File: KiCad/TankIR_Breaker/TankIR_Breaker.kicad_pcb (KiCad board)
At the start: 2 copper layers, 44.6 x 18.2 mm, 16 parts, among them J1 VBATT, J2 TRIGGER, J3 SERVO, J4 RC, J5 APPLE, J6 SOUND, J7 IR_OUT, J8 MUZZLE, Q1 BC337, Q2 BC337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

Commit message: upd
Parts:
- moved R3 0.20 mm to (116.1, 70.7)
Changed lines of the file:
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@@
 	(footprint "Resistor_THT:R_Axial_DIN0204_L3.6mm_D1.6mm_P2.54mm_Vertical"
 		(layer "F.Cu")
-		(at 116.12 70.5 180)
+		(at 116.12 70.7 180)
 		(descr "Resistor, Axial_DIN0204 series, Axial, Vertical, pin pitch=2.54mm, 0.167W, length*diameter=3.6*1.6mm^2, http://cdn-reichelt.de/documents/datenblatt/B400/1_4W%23YAG.pdf")
 		(tags "Resistor Axial_DIN0204 series Axial Vertical pin pitch 2.54mm 0.167W length 3.6mm diameter 1.6mm")
 		(property "Reference" "R3"
-			(at 3.22 2 270)
+			(at 3.42 1.3 180)
 			(layer "F.SilkS")
 			(effects
@@
 		)
 	)
+	(gr_text "+"
+		(at 113.1 69 0)
+		(layer "F.SilkS")
+		(effects
+			(font
+				(size 1 1)
+				(thickness 0.2)
+				(bold yes)
+			)
+			(justify left bottom)
+		)
+	)
 	(gr_text "TRIG"
 		(at 92.1 63.1 90)
@@
 	)
 	(gr_text "+"
-		(at 96.4 63.9 0)
+		(at 90.7 64 0)
 		(layer "F.SilkS")
 		(effects

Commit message: fix
Fixed missing 5V connection
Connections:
- A1 pad 27: unconnected-(A1-+5V-Pad27) -> 5V

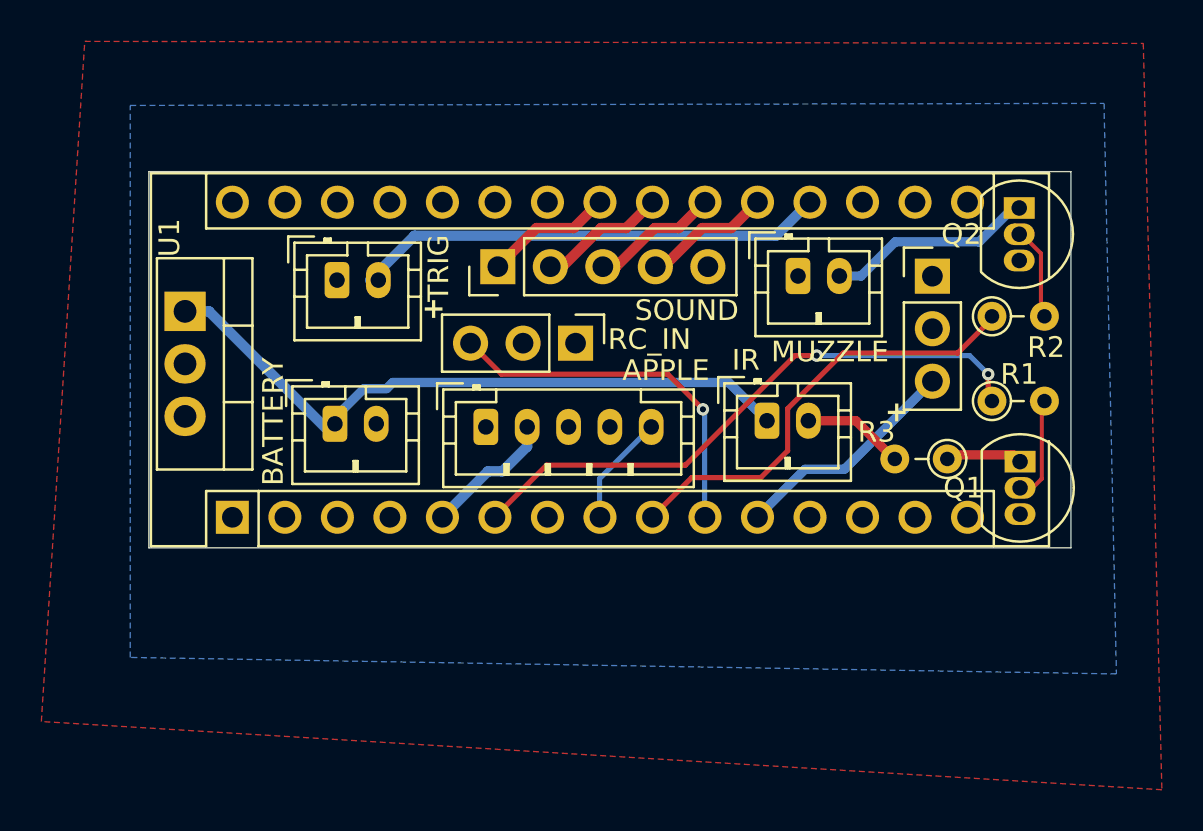
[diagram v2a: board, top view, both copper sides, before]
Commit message: REV2
Modified board for more reliable fabrication and added Pull-down resistors to avoid Transistor current leakage
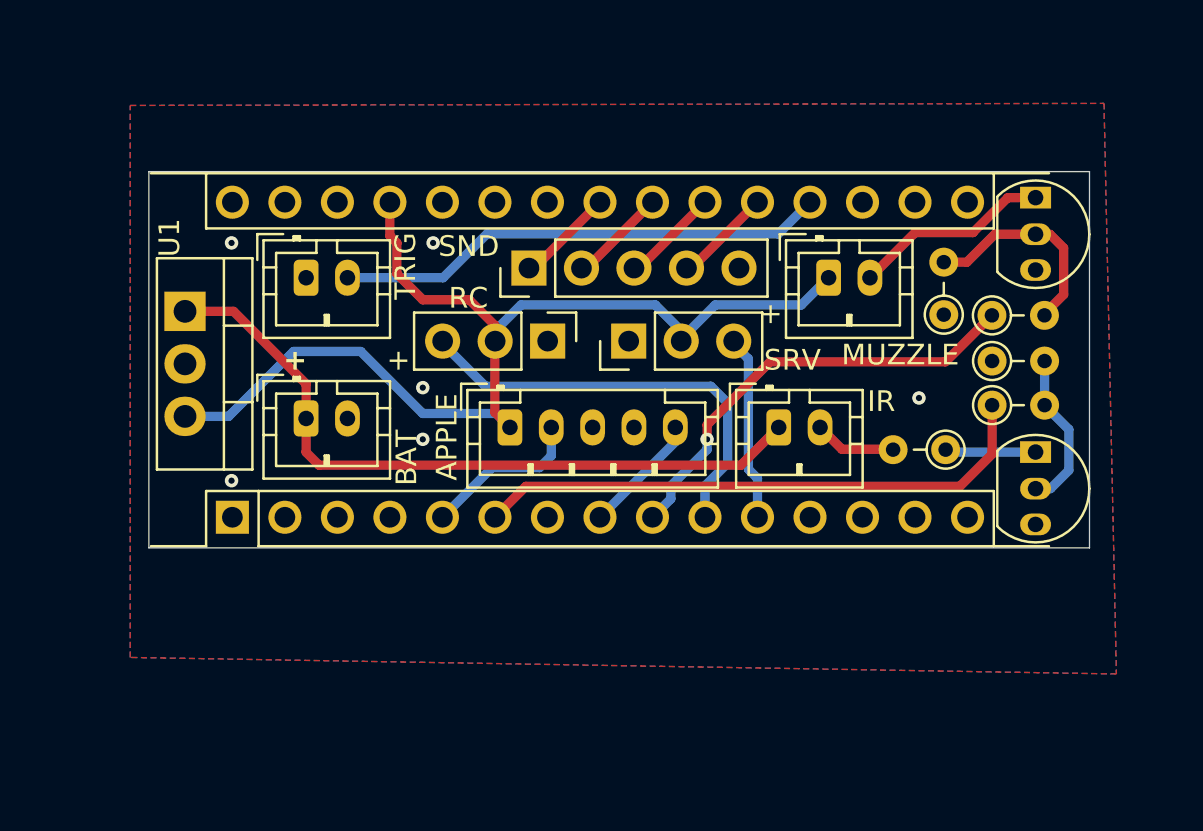
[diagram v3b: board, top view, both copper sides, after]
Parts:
- removed the ? at (87.0, 65.9)
- added ?: , FHD-KiCad-LOGOS:LOGO-SR, B.Cu at (87.5, 65.5)
- added R4: 10K, Resistor_THT:R_Axial_DIN0204_L3.6mm_D1.6mm_P2.54mm_Vertical, F.Cu at (118.3, 66.0)
- added R5: 10K, Resistor_THT:R_Axial_DIN0204_L3.6mm_D1.6mm_P2.54mm_Vertical, F.Cu at (116.0, 63.7)
- moved J3 15.0 mm to (100.7, 65.0), turned to 90 degrees
- moved J6 1.51 mm to (95.9, 61.5)
- moved J2 1.50 mm to (85.1, 61.9)
- moved J8 1.48 mm to (110.4, 61.9)
- moved J1 1.42 mm to (85.1, 68.7)
- moved J4 1.35 mm to (96.8, 65.0)
- moved J5 1.17 mm to (95.0, 69.2)
- moved Q2 0.79 mm to (120.4, 58.6)
- moved Q1 0.75 mm to (120.4, 70.9)
- moved J7 0.65 mm to (108.0, 69.2)
- moved R3 0.46 mm to (116.0, 70.2)
- moved R1 0.20 mm to (118.3, 68.1)
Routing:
- net 5V: track 0.00 -> 52.8 mm
- net Net-(Q2-B): track 5.24 -> 10.3 mm
- net /RC_IN: track 17.8 -> 21.0 mm, vias 1 -> 0
- net Net-(Q1-B): track 5.19 -> 8.13 mm
- net /Recoil_OUT: track 11.2 -> 9.02 mm
- net +BATT: track 32.4 -> 34.5 mm
- net /SOUND_REP: track 6.21 -> 4.76 mm
- net /SOUND_HIT: track 6.21 -> 4.76 mm
- net /SOUND_FIRE: track 6.21 -> 4.76 mm
- net /SOUND_DES: track 6.21 -> 4.76 mm
- net /IR_IN: track 6.49 -> 7.87 mm
- net Net-(J8-Pin_2): track 10.1 -> 8.83 mm
- net /IR OUT: track 28.8 -> 27.7 mm, vias 2 -> 0
- net /Trigger: track 22.8 -> 23.9 mm
- net Net-(Q1-C): track 3.33 -> 4.06 mm
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- added copper zone on F.Cu, net GND
- removed copper zone on F.Cu, net 5V
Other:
- board size 44.6 x 18.2 mm -> 45.5 x 18.2 mm
- board text added: "BAT"
- board text added: "D"
- board text added: "F"
- board text added: "FHD.26"
- board text added: "G"
- board text added: "H"
- board text added: "R"
- board text added: "RC"
- board text added: "REV.2"
- board text added: "SND"
- board text added: "SRV"
- board text added: "TankIR_HAT"
- board text added: "V"
- board text removed: "BATTERY"
- board text removed: "RC_IN"
- board text removed: "SERVO"
- board text removed: "SOUND"
- board text removed: "TankIR_HAT FHD 2026"

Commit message: Correction
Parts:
- R1, R2: value R -> 200
- R3: value R -> 3.3
- R4, R5: value 10K -> 2.2k
- moved J4 5.08 mm to (91.7, 65.0), turned to 90 degrees
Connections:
- R4 pad 2: Net-(Q1-B) -> /IR OUT
- R5 pad 2: Net-(Q2-B) -> /MUZZLE
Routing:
- net /RC_IN: track 21.0 -> 15.9 mm
- net Net-(Q2-B): track 10.3 -> 6.38 mm
- net /MUZZLE: track 21.5 -> 25.4 mm
- net /IR OUT: track 27.7 -> 31.1 mm
- net Net-(Q1-B): track 8.13 -> 5.99 mm
- net Net-(J8-Pin_2): track 8.83 -> 9.62 mm
- net GND: vias 6 -> 7
